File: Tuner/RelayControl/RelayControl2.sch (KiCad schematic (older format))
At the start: 69 parts, among them J3 Conn_01x06, J4 Conn_02x16_Odd_Even, J5 Conn_01x01, J6 Conn_01x01, J7 Conn_01x01, J8 Conn_01x01, U4 MCP23017, U5 ULN2803A, U6 ULN2803A

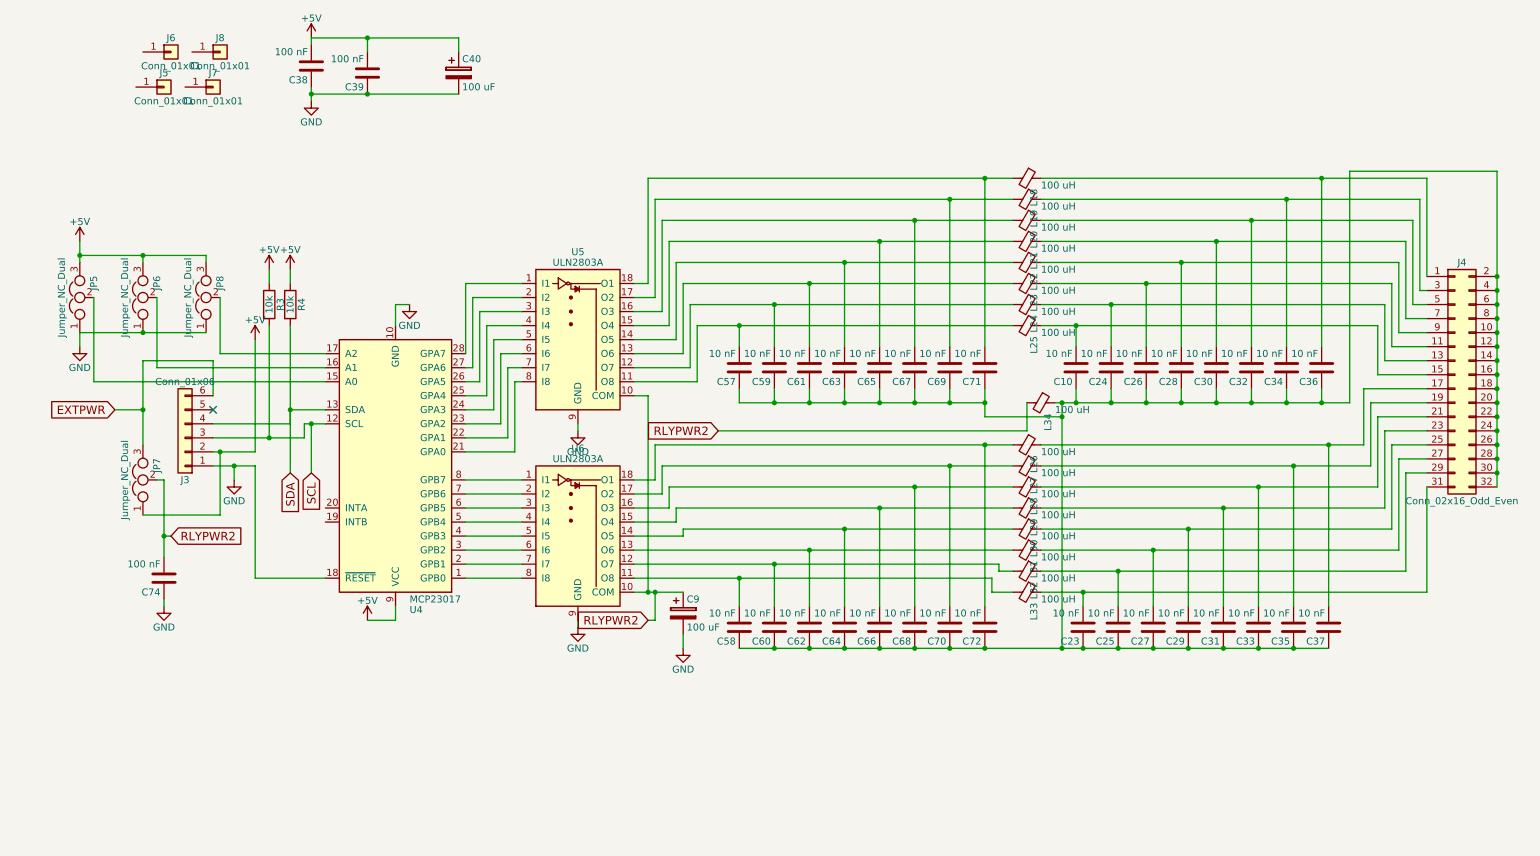
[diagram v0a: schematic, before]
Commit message: Modified RelayControl and Reversible Section to Isolate Digital from Analog sections using RF chokes
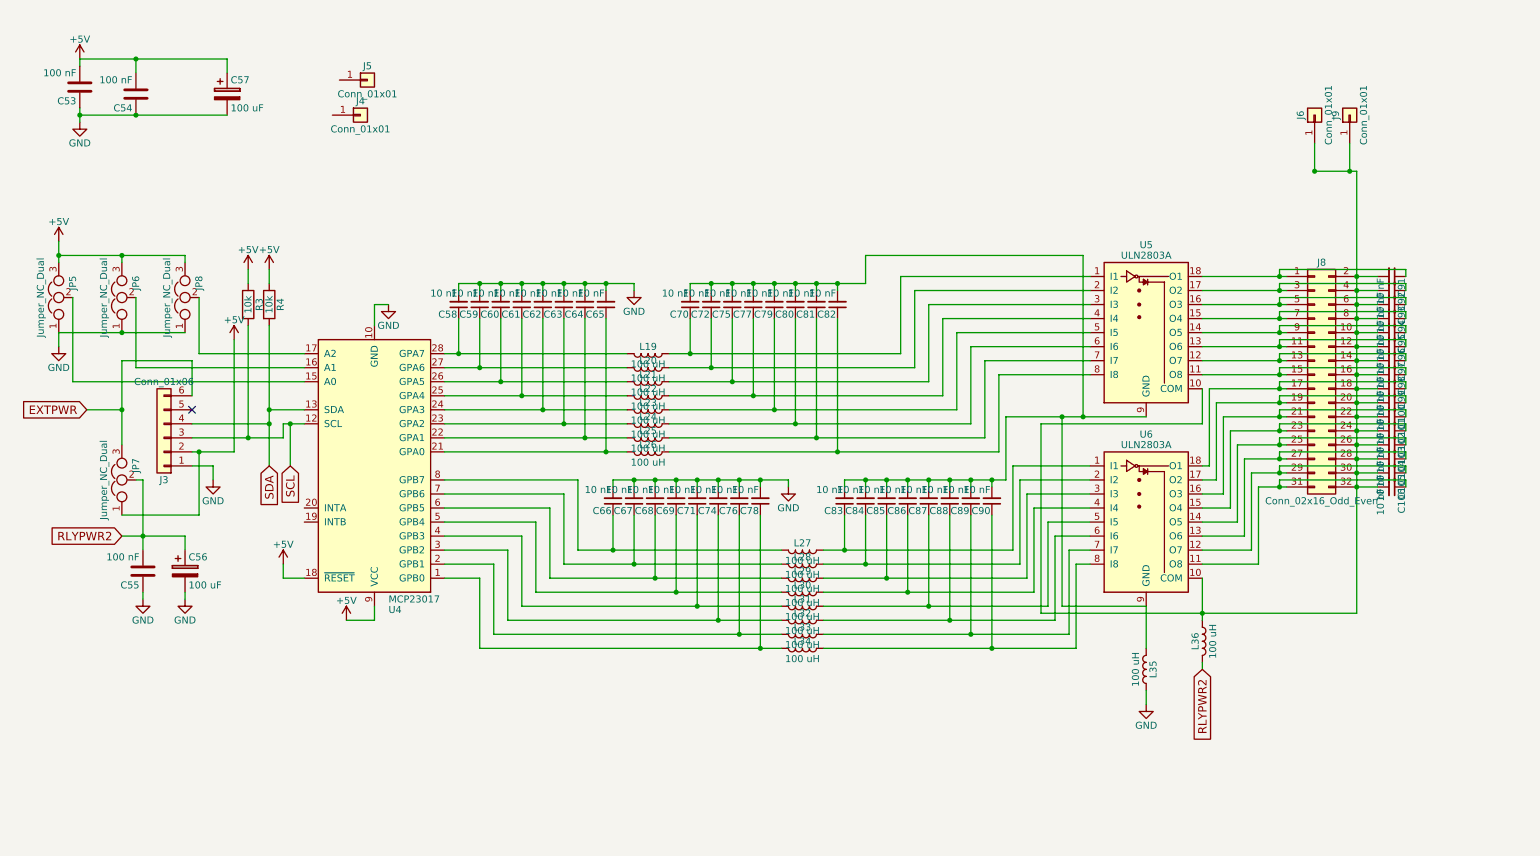
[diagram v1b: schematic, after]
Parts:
- removed C10, C23, C24, C25, C26, C27, C28, C29, C30, C31, C32, C33, C34, C35, C36, C37, C57, C58, C59, C60, C61, C62, C63, C64, C65, C66, C67, C68, C69, C70, C71, C72: 10 nF, Capacitors_THT:C_Disc_D5.0mm_W2.5mm_P2.50mm, symbol C
- removed C38, C39, C74: 100 nF, Capacitors_THT:C_Disc_D5.0mm_W2.5mm_P2.50mm, symbol C
- removed C40, C9: 100 uF, Capacitors_THT:CP_Radial_D8.0mm_P5.00mm, symbol CP
- removed J4: Conn_02x16_Odd_Even, Pin_Headers:Pin_Header_Straight_2x16_Pitch2.54mm, symbol Conn_02x16_Odd_Even
- removed J7, J8: Conn_01x01, Connectors:1pin, symbol Conn_01x01
- removed L18, L19, L20, L21, L22, L23, L24, L25, L26, L27, L28, L29, L30, L31, L32, L33, L34: 100 uH, Inductors_THT:L_Axial_L5.3mm_D2.2mm_P7.62mm_Horizontal_Vishay_IM-1, symbol Ferrite_Bead_Small
- added C100, C101, C102, C103, C104, C105, C106, C58, C59, C60, C61, C62, C63, C64, C65, C66, C67, C68, C69, C70, C71, C72, C74, C75, C76, C77, C78, C79, C80, C81, C82, C83, C84, C85, C86, C87, C88, C89, C90, C91, C92, C93, C94, C95, C96, C97, C98, C99: 10 nF, Capacitors_THT:C_Disc_D5.0mm_W2.5mm_P2.50mm, symbol C_Small
- added C53, C54, C55: 100 nF, Capacitors_THT:C_Disc_D5.0mm_W2.5mm_P2.50mm, symbol C
- added C56, C57: 100 uF, Capacitors_THT:CP_Radial_D8.0mm_P5.00mm, symbol CP
- added J4, J9: Conn_01x01, Connectors:1pin, symbol Conn_01x01
- added J8: Conn_02x16_Odd_Even, Pin_Headers:Pin_Header_Straight_2x16_Pitch2.54mm, symbol Conn_02x16_Odd_Even
- added L19, L20, L21, L22, L23, L24, L25, L26, L27, L28, L29, L30, L31, L32, L33, L34, L35, L36: 100 uH, Inductors_THT:L_Axial_L5.3mm_D2.2mm_P7.62mm_Horizontal_Vishay_IM-1, symbol L
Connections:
- net +5V: now also U4.18 (~RESET), C53.2, C54.2, C57.1
- net GND: now also C53.1, C54.1, C55.1, C56.2, C57.2, C58.2, C59.2, C60.2, C61.2, C62.2, C63.2, C64.2, C65.2, C66.2, C67.2, C68.2, C69.2, C71.2, C74.2, C76.2, C78.2, L35.1; no longer U4.18 (~RESET), U5.9 (GND), U6.9 (GND)
- net RLYPWR2: now also C55.2, C56.1, L36.2; no longer U5.10 (COM), U6.10 (COM)
- net at U5.1 (I1): now also C70.1, L19.1; no longer U4.28 (GPA7)
- net at U5.11 (O8): now also C98.1, J8.15 (Pin_15)
- net at U5.12 (O7): now also C97.1, J8.13 (Pin_13)
- net at U5.13 (O6): now also C96.1, J8.11 (Pin_11)
- net at U5.14 (O5): now also C95.1, J8.9 (Pin_9)
- net at U5.15 (O4): now also C94.1, J8.7 (Pin_7)
- net at U5.16 (O3): now also C93.1, J8.5 (Pin_5)
- net at U5.17 (O2): now also C92.1, J8.3 (Pin_3)
- net at U5.18 (O1): now also C91.1, J8.1 (Pin_1)
- net at U5.2 (I2): now also C72.1, L20.1; no longer U4.27 (GPA6)
- net at U5.3 (I3): now also C75.1, L21.1; no longer U4.26 (GPA5)
- net at U5.4 (I4): now also C77.1, L22.1; no longer U4.25 (GPA4)
- net at U5.5 (I5): now also C79.1, L23.1; no longer U4.24 (GPA3)
- net at U5.6 (I6): now also C80.1, L24.1; no longer U4.23 (GPA2)
- net at U5.7 (I7): now also C81.1, L25.1; no longer U4.22 (GPA1)
- net at U5.8 (I8): now also C82.1, L26.1; no longer U4.21 (GPA0)
- net at J6.1 (Pin_1): now also U5.10 (COM), U6.10 (COM), C100.2, C101.2, C102.2, C103.2, C104.2, C105.2, C106.2, C91.2, C92.2, C93.2, C94.2, C95.2, C96.2, C97.2, C98.2, C99.2, J8.10 (Pin_10), J8.12 (Pin_12), J8.14 (Pin_14), J8.16 (Pin_16), J8.18 (Pin_18), J8.2 (Pin_2), J8.20 (Pin_20), J8.22 (Pin_22), J8.24 (Pin_24), J8.26 (Pin_26), J8.28 (Pin_28), J8.30 (Pin_30), J8.32 (Pin_32), J8.4 (Pin_4), J8.6 (Pin_6), J8.8 (Pin_8), J9.1 (Pin_1), L36.1
- net at U4.1 (GPB0): now also C78.1, L34.2; no longer U6.8 (I8)
- net at U4.2 (GPB1): now also C76.1, L33.2; no longer U6.7 (I7)
- net at U4.3 (GPB2): now also C74.1, L32.2; no longer U6.6 (I6)
- net at U4.4 (GPB3): now also C71.1, L31.2; no longer U6.5 (I5)
- net at U4.5 (GPB4): now also C69.1, L30.2; no longer U6.4 (I4)
- net at U4.6 (GPB5): now also C68.1, L29.2; no longer U6.3 (I3)
- net at U4.7 (GPB6): now also C67.1, L28.2; no longer U6.2 (I2)
- net at U4.8 (GPB7): now also C66.1, L27.2; no longer U6.1 (I1)
- net at U6.11 (O8): now also C106.1, J8.31 (Pin_31)
- net at U6.12 (O7): now also C105.1, J8.29 (Pin_29)
- net at U6.13 (O6): now also C104.1, J8.27 (Pin_27)
- net at U6.14 (O5): now also C103.1, J8.25 (Pin_25)
- net at U6.15 (O4): now also C102.1, J8.23 (Pin_23)
- net at U6.16 (O3): now also C101.1, J8.21 (Pin_21)
- net at U6.17 (O2): now also C100.1, J8.19 (Pin_19)
- net at U6.18 (O1): now also C99.1, J8.17 (Pin_17)
- new net: C70.2, C72.2, C75.2, C77.2, C79.2, C80.2, C81.2, C82.2, C83.2, C84.2, C85.2, C86.2, C87.2, C88.2, C89.2, C90.2, L35.2, U5.9 (GND), U6.9 (GND)
- new net: C65.1, L26.2, U4.21 (GPA0)
- new net: C64.1, L25.2, U4.22 (GPA1)
- new net: C63.1, L24.2, U4.23 (GPA2)
- new net: C62.1, L23.2, U4.24 (GPA3)
- new net: C61.1, L22.2, U4.25 (GPA4)
- new net: C60.1, L21.2, U4.26 (GPA5)
- new net: C59.1, L20.2, U4.27 (GPA6)
- new net: C58.1, L19.2, U4.28 (GPA7)
- new net: C83.1, L27.1, U6.1 (I1)
- new net: C84.1, L28.1, U6.2 (I2)
- new net: C85.1, L29.1, U6.3 (I3)
- new net: C86.1, L30.1, U6.4 (I4)
- new net: C87.1, L31.1, U6.5 (I5)
- new net: C88.1, L32.1, U6.6 (I6)
- new net: C89.1, L33.1, U6.7 (I7)
- new net: C90.1, L34.1, U6.8 (I8)

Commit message: Added extra filtering and shunt to RF ground
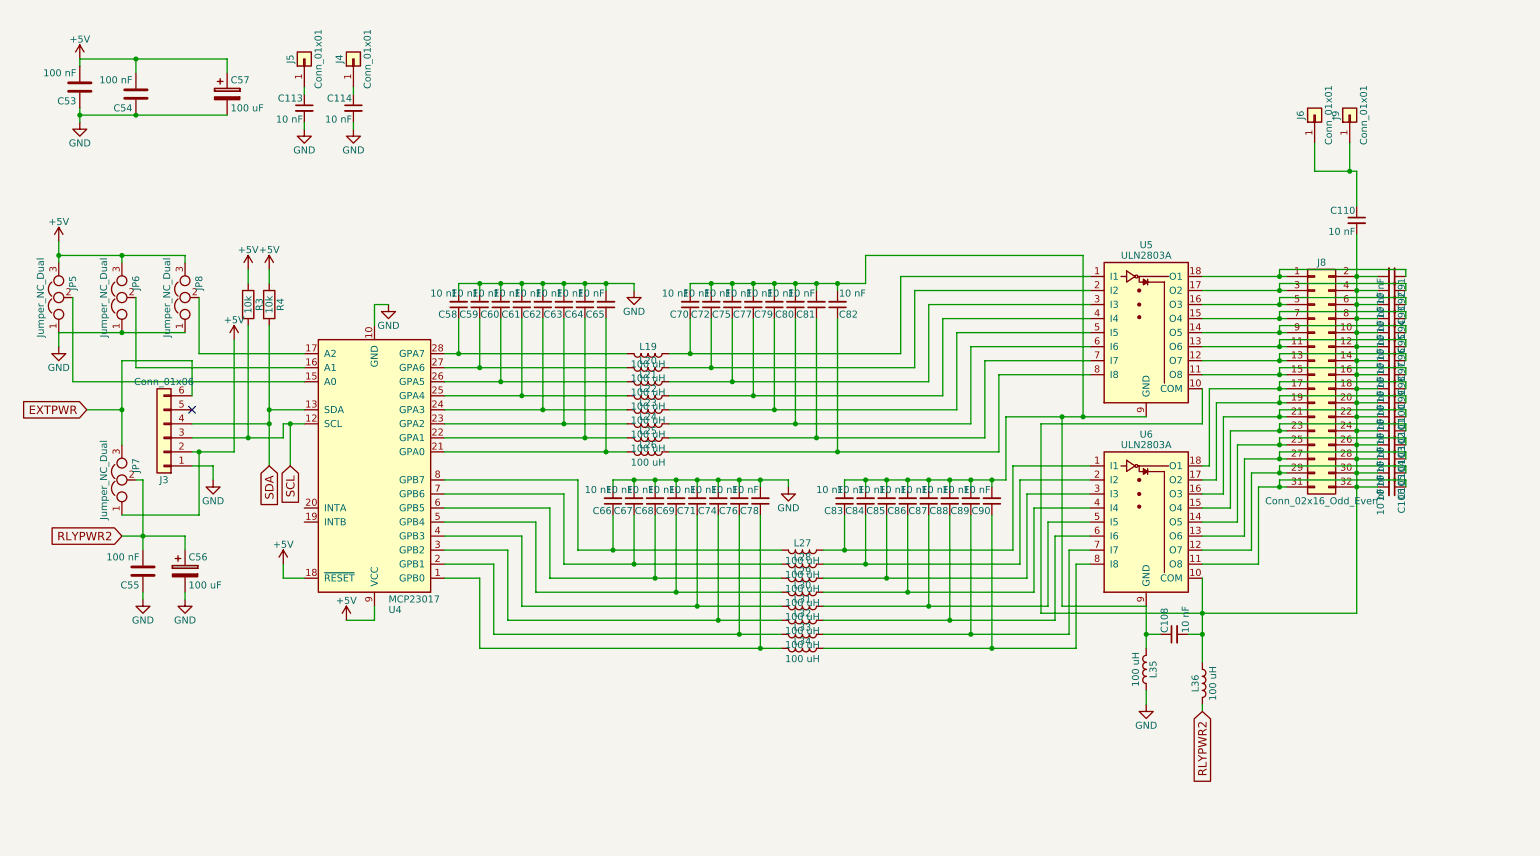
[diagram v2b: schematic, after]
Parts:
- added C108, C110, C113, C114: 10 nF, Capacitors_THT:C_Disc_D5.0mm_W2.5mm_P2.50mm, symbol C_Small
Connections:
- net GND: now also C113.2, C114.2
- net at C100.2, C101.2, C102.2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: now also C108.2, C110.2; no longer J6.1 (Pin_1), J9.1 (Pin_1)
- net at C70.2, C72.2, C75.2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: now also C108.1
- net at J5.1 (Pin_1): now also C113.1
- net at J4.1 (Pin_1): now also C114.1
- new net: C110.1, J6.1 (Pin_1), J9.1 (Pin_1)
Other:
- moved on the sheet: J4, J5, L36
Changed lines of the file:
@@
 $EndComp
 $Comp
-L +5V #PWR19
+L +5V #PWR21
 U 1 1 5B99E946
 P 1050 1050
-F 0 "#PWR19" H 1050 900 50  0001 C CNN
+F 0 "#PWR21" H 1050 900 50  0001 C CNN
 F 1 "+5V" H 1050 1190 50  0000 C CNN
 F 2 "" H 1050 1050 50  0001 C CNN
@@
 $EndComp
 $Comp
-L GND #PWR20
+L GND #PWR22
 U 1 1 5B99E94C
 P 1050 1500
-F 0 "#PWR20" H 1050 1250 50  0001 C CNN
+F 0 "#PWR22" H 1050 1250 50  0001 C CNN
 F 1 "GND" H 1050 1350 50  0000 C CNN
 F 2 "" H 1050 1500 50  0001 C CNN
@@
 L Conn_01x01 J5
 U 1 1 5B99E960
-P 3100 1200
-F 0 "J5" H 3100 1300 50  0000 C CNN
-F 1 "Conn_01x01" H 3100 1100 50  0000 C CNN
-F 2 "Connectors:1pin" H 3100 1200 50  0001 C CNN
-F 3 "" H 3100 1200 50  0001 C CNN
-	1    3100 1200
-	1    0    0    -1
+P 2650 1050
+F 0 "J5" H 2650 1150 50  0000 C CNN
+F 1 "Conn_01x01" H 2650 950 50  0000 C CNN
+F 2 "Connectors:1pin" H 2650 1050 50  0001 C CNN
+F 3 "" H 2650 1050 50  0001 C CNN
+	1    2650 1050
+	0    -1   -1   0
 $EndComp
 $Comp
@@
 L Conn_01x01 J4
 U 1 1 5B99E96E
-P 3050 1450
-F 0 "J4" H 3050 1550 50  0000 C CNN
-F 1 "Conn_01x01" H 3050 1350 50  0000 C CNN
-F 2 "Connectors:1pin" H 3050 1450 50  0001 C CNN
-F 3 "" H 3050 1450 50  0001 C CNN
-	1    3050 1450
-	1    0    0    -1
+P 3000 1050
+F 0 "J4" H 3000 1150 50  0000 C CNN
+F 1 "Conn_01x01" H 3000 950 50  0000 C CNN
+F 2 "Connectors:1pin" H 3000 1050 50  0001 C CNN
+F 3 "" H 3000 1050 50  0001 C CNN
+	1    3000 1050
+	0    -1   -1   0
 $EndComp
 $Comp
@@
 $EndComp
 $Comp
-L GND #PWR18
+L GND #PWR20
 U 1 1 5B99E9A6
 P 900 3100
-F 0 "#PWR18" H 900 2850 50  0001 C CNN
+F 0 "#PWR20" H 900 2850 50  0001 C CNN
 F 1 "GND" H 900 2950 50  0000 C CNN
 F 2 "" H 900 3100 50  0001 C CNN
@@
 $EndComp
 $Comp
-L +5V #PWR17
+L +5V #PWR19
 U 1 1 5B99E9AC
 P 900 2350
-F 0 "#PWR17" H 900 2200 50  0001 C CNN
+F 0 "#PWR19" H 900 2200 50  0001 C CNN
 F 1 "+5V" H 900 2490 50  0000 C CNN
 F 2 "" H 900 2350 50  0001 C CNN
@@
 $EndComp
 $Comp
-L GND #PWR23
+L GND #PWR25
 U 1 1 5B99E9B2
 P 2000 4050
-F 0 "#PWR23" H 2000 3800 50  0001 C CNN
+F 0 "#PWR25" H 2000 3800 50  0001 C CNN
 F 1 "GND" H 2000 3900 50  0000 C CNN
 F 2 "" H 2000 4050 50  0001 C CNN
@@
 $EndComp
 $Comp
-L +5V #PWR24
+L +5V #PWR26
 U 1 1 5B99E9B8
 P 2150 3050
-F 0 "#PWR24" H 2150 2900 50  0001 C CNN
+F 0 "#PWR26" H 2150 2900 50  0001 C CNN
 F 1 "+5V" H 2150 3190 50  0000 C CNN
 F 2 "" H 2150 3050 50  0001 C CNN
@@
 $EndComp
 $Comp
-L +5V #PWR26
+L +5V #PWR28
 U 1 1 5B99E9C5
 P 2400 2550
-F 0 "#PWR26" H 2400 2400 50  0001 C CNN
+F 0 "#PWR28" H 2400 2400 50  0001 C CNN
 F 1 "+5V" H 2400 2690 50  0000 C CNN
 F 2 "" H 2400 2550 50  0001 C CNN
@@
 $EndComp
 $Comp
-L +5V #PWR25
+L +5V #PWR27
 U 1 1 5B99E9D2
 P 2250 2550
-F 0 "#PWR25" H 2250 2400 50  0001 C CNN
+F 0 "#PWR27" H 2250 2400 50  0001 C CNN
 F 1 "+5V" H 2250 2690 50  0000 C CNN
 F 2 "" H 2250 2550 50  0001 C CNN
@@
 $EndComp
 $Comp
-L GND #PWR29
+L GND #PWR33
 U 1 1 5B99E9DF
 P 3250 2800
-F 0 "#PWR29" H 3250 2550 50  0001 C CNN
+F 0 "#PWR33" H 3250 2550 50  0001 C CNN
 F 1 "GND" H 3250 2650 50  0000 C CNN
 F 2 "" H 3250 2800 50  0001 C CNN
@@
 RLYPWR2
 $Comp
-L +5V #PWR28
+L +5V #PWR31
 U 1 1 5B99E9F5
 P 2950 5050
-F 0 "#PWR28" H 2950 4900 50  0001 C CNN
+F 0 "#PWR31" H 2950 4900 50  0001 C CNN
 F 1 "+5V" H 2950 5190 50  0000 C CNN
 F 2 "" H 2950 5050 50  0001 C CNN
@@
 $EndComp
 $Comp
-L GND #PWR22
+L GND #PWR24
 U 1 1 5B99E9FB
 P 1800 4900
-F 0 "#PWR22" H 1800 4650 50  0001 C CNN
+F 0 "#PWR24" H 1800 4650 50  0001 C CNN
 F 1 "GND" H 1800 4750 50  0000 C CNN
 F 2 "" H 1800 4900 50  0001 C CNN
@@
 $EndComp
 $Comp
-L GND #PWR21
+L GND #PWR23
 U 1 1 5B99EA0B
 P 1500 4900
-F 0 "#PWR21" H 1500 4650 50  0001 C CNN
+F 0 "#PWR23" H 1500 4650 50  0001 C CNN
 F 1 "GND" H 1500 4750 50  0000 C CNN
 F 2 "" H 1500 4900 50  0001 C CNN
@@
 $EndComp
 $Comp
-L +5V #PWR27
+L +5V #PWR29
 U 1 1 5B99EA11
 P 2500 4650
-F 0 "#PWR27" H 2500 4500 50  0001 C CNN
+F 0 "#PWR29" H 2500 4500 50  0001 C CNN
 F 1 "+5V" H 2500 4790 50  0000 C CNN
 F 2 "" H 2500 4650 50  0001 C CNN
@@
 $EndComp
 $Comp
-L GND #PWR32
+L GND #PWR36
 U 1 1 5B99EA17
 P 8650 5650
-F 0 "#PWR32" H 8650 5400 50  0001 C CNN
+F 0 "#PWR36" H 8650 5400 50  0001 C CNN
 F 1 "GND" H 8650 5500 50  0000 C CNN
 F 2 "" H 8650 5650 50  0001 C CNN
@@
 L L L36
 U 1 1 5B99EA8D
-P 9050 5200
-F 0 "L36" V 9000 5200 50  0000 C CNN
-F 1 "100 uH" V 9125 5200 50  0000 C CNN
-F 2 "Inductors_THT:L_Axial_L5.3mm_D2.2mm_P7.62mm_Horizontal_Vishay_IM-1" H 9050 5200 50  0001 C CNN
-F 3 "" H 9050 5200 50  0001 C CNN
-	1    9050 5200
-	1    0    0    -1
-$EndComp
-Text GLabel 9050 5400 3    60   Input ~ 0
+P 9050 5500
+F 0 "L36" V 9000 5500 50  0000 C CNN
+F 1 "100 uH" V 9125 5500 50  0000 C CNN
+F 2 "Inductors_THT:L_Axial_L5.3mm_D2.2mm_P7.62mm_Horizontal_Vishay_IM-1" H 9050 5500 50  0001 C CNN
+F 3 "" H 9050 5500 50  0001 C CNN
+	1    9050 5500
+	1    0    0    -1
+$EndComp
+Text GLabel 9050 5700 3    60   Input ~ 0
 RLYPWR2
 $Comp
@@
 $EndComp
 $Comp
-L GND #PWR30
+L GND #PWR34
 U 1 1 5B99EB13
 P 5000 2700
-F 0 "#PWR30" H 5000 2450 50  0001 C CNN
+F 0 "#PWR34" H 5000 2450 50  0001 C CNN
 F 1 "GND" H 5000 2550 50  0000 C CNN
 F 2 "" H 5000 2700 50  0001 C CNN
@@
 F 3 "" H 6450 2800 50  0001 C CNN
 	1    6450 2800
-	-1   0    0    1
+	1    0    0    1
 $EndComp
 $Comp
@@
 $EndComp
 $Comp
-L GND #PWR31
+L GND #PWR35
 U 1 1 5B99EBC1
 P 6100 4100
-F 0 "#PWR31" H 6100 3850 50  0001 C CNN
+F 0 "#PWR35" H 6100 3850 50  0001 C CNN
 F 1 "GND" H 6100 3950 50  0000 C CNN
 F 2 "" H 6100 4100 50  0001 C CNN
@@
 Connection ~ 10150 4100
 Wire Wire Line
-	9050 4750 9050 5050
+	9050 4750 9050 5350
 Wire Wire Line
 	10150 5000 7900 5000
@@
 Wire Wire Line
 	9050 2600 9650 2600
-Connection ~ 9850 1850
 Wire Wire Line
 	9850 1850 9850 1650
-Connection ~ 10100 1850
 Wire Wire Line
 	10100 1650 10100 1850
@@
 Connection ~ 10150 2700
 Wire Wire Line
-	10150 1850 10150 5000
+	10150 2300 10150 5000
 Wire Wire Line
 	3150 5050 3150 4950
@@
 	8650 5650 8650 5550
 Wire Wire Line
-	9050 5350 9050 5400
+	9050 5650 9050 5700
 Wire Wire Line
 	7950 4950 7950 4350
@@
 	2400 2950 2400 3950
 Connection ~ 2400 3650
+$Comp
+L C_Small C108
+U 1 1 5B9714C9
+P 8850 5150
+F 0 "C108" H 8860 5220 50  0000 L CNN
+F 1 "10 nF" H 8860 5070 50  0000 L CNN
+F 2 "Capacitors_THT:C_Disc_D5.0mm_W2.5mm_P2.50mm" H 8850 5150 50  0001 C CNN
+F 3 "" H 8850 5150 50  0001 C CNN
+	1    8850 5150
+	0    -1   -1   0
+$EndComp
+Wire Wire Line
+	8950 5150 9050 5150
+Connection ~ 9050 5150
+Wire Wire Line
+	8750 5150 8650 5150
+Connection ~ 8650 5150
+$Comp
+L C_Small C110
+U 1 1 5B97C0E4
+P 10150 2200
+F 0 "C110" H 10160 2270 50  0000 L CNN
+F 1 "10 nF" H 10160 2120 50  0000 L CNN
+F 2 "Capacitors_THT:C_Disc_D5.0mm_W2.5mm_P2.50mm" H 10150 2200 50  0001 C CNN
+F 3 "" H 10150 2200 50  0001 C CNN
+	1    10150 2200
+	-1   0    0    -1
+$EndComp
+Wire Wire Line
+	10150 1850 10150 2100
+Connection ~ 10100 1850
+$Comp
+L GND #PWR30
+U 1 1 5B97DFC4
+P 2650 1550
+F 0 "#PWR30" H 2650 1300 50  0001 C CNN
+F 1 "GND" H 2650 1400 50  0000 C CNN
+F 2 "" H 2650 1550 50  0001 C CNN
+F 3 "" H 2650 1550 50  0001 C CNN
+	1    2650 1550
+	1    0    0    -1
+$EndComp
+$Comp
+L C_Small C113
+U 1 1 5B97E187
+P 2650 1400
+F 0 "C113" H 2660 1470 50  0000 L CNN
+F 1 "10 nF" H 2660 1320 50  0000 L CNN
+F 2 "Capacitors_THT:C_Disc_D5.0mm_W2.5mm_P2.50mm" H 2650 1400 50  0001 C CNN
+F 3 "" H 2650 1400 50  0001 C CNN
+	1    2650 1400
+	-1   0    0    -1
+$EndComp
+Wire Wire Line
+	2650 1250 2650 1300
+Wire Wire Line
+	2650 1500 2650 1550
+$Comp
+L C_Small C114
+U 1 1 5B97F00E
+P 3000 1400
+F 0 "C114" H 3010 1470 50  0000 L CNN
+F 1 "10 nF" H 3010 1320 50  0000 L CNN
+F 2 "Capacitors_THT:C_Disc_D5.0mm_W2.5mm_P2.50mm" H 3000 1400 50  0001 C CNN
+F 3 "" H 3000 1400 50  0001 C CNN
+	1    3000 1400
+	-1   0    0    -1
+$EndComp
+$Comp
+L GND #PWR32
+U 1 1 5B97F132
+P 3000 1550
+F 0 "#PWR32" H 3000 1300 50  0001 C CNN
+F 1 "GND" H 3000 1400 50  0000 C CNN
+F 2 "" H 3000 1550 50  0001 C CNN
+F 3 "" H 3000 1550 50  0001 C CNN
+	1    3000 1550
+	1    0    0    -1
+$EndComp
+Wire Wire Line
+	3000 1500 3000 1550
+Wire Wire Line
+	3000 1250 3000 1300
 $EndSCHEMATC
